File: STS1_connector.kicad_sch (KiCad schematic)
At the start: 2 parts

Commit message: Label RasPi Zero W pin header
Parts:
- added J2, J3: Conn_02x20_Odd_Even, symbol Connector_Generic:Conn_02x20_Odd_Even
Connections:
- net GND: now also J2.10 (Pin_10), J2.13 (Pin_13), J2.19 (Pin_19), J2.26 (Pin_26), J2.29 (Pin_29), J2.33 (Pin_33), J2.40 (Pin_40), J2.5 (Pin_5), J3.10 (Pin_10), J3.13 (Pin_13), J3.19 (Pin_19), J3.26 (Pin_26), J3.29 (Pin_29), J3.33 (Pin_33), J3.40 (Pin_40), J3.5 (Pin_5)
- new net 3V3: J2.2 (Pin_2), J3.18 (Pin_18), J3.2 (Pin_2)
- new net 5V: J3.1 (Pin_1), J3.3 (Pin_3)
- new net GPIO17: J2.12 (Pin_12), J3.12 (Pin_12)
- new net GPIO22: J2.16 (Pin_16), J3.16 (Pin_16)
- new net GPIO27: J2.14 (Pin_14), J3.14 (Pin_14)
- new net RX: J3.9 (Pin_9)
- new net SCL0: J2.6 (Pin_6)
- new net SDA0: J2.4 (Pin_4)
- new net TX: J3.7 (Pin_7)
- no-connect marks 0 -> 49
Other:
- note added: "CSBI connectors"
- note added: "EDU CSBI [1]"
- note added: "Pi HAT [2]"
- note added: "Pi HAT connector"
- note added: "Pi Zero W [3]"
- note added: "Pi Zero W connector"
- note added: "[1] https://github.com/SpaceTeam/STS1_EDU_Hardware [2] https://github.com/SpaceTeam/EDU_RASPI_HATS [3] https://pip-assets.raspberrypi.com/categories/592-raspberry-pi-zero-w/documents/RP-008368-DS-1-raspberry-pi-zero-w-reduced-schematics.pdf"

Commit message: Add 3V3 LDO: could be used to set EPS_BAT_GOOD high
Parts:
- J1: renamed from J2; footprint (none) -> Connector_PinHeader_2.00mm:PinHeader_2x20_P2.00mm_Vertical
- J2: renamed from J3; footprint (none) -> Connector_PinHeader_2.00mm:PinHeader_2x20_P2.00mm_Vertical

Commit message: Clean-up
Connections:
- net 3V3 renamed Pi_3V3
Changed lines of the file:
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@@
 		)
 	)
-	(global_label "3V3"
+	(global_label "Pi_3V3"
 		(shape input)
 		(at 242.57 44.45 0)
@@
 		)
 		(property "Intersheetrefs" "${INTERSHEET_REFS}"
-			(at 248.4086 44.45 0)
+			(at 251.251 44.45 0)
 			(hide yes)
 			(show_name no)
@@
 		)
 	)
-	(global_label "3V3"
+	(global_label "Pi_3V3"
 		(shape input)
 		(at 185.42 44.45 0)
@@
 		)
 		(property "Intersheetrefs" "${INTERSHEET_REFS}"
-			(at 191.2586 44.45 0)
+			(at 194.101 44.45 0)
 			(hide yes)
 			(show_name no)
@@
 		)
 	)
-	(global_label "3V3"
+	(global_label "Pi_3V3"
 		(shape input)
 		(at 242.57 64.77 0)
@@
 		)
 		(property "Intersheetrefs" "${INTERSHEET_REFS}"
-			(at 248.4086 64.77 0)
-			(hide yes)
-			(show_name no)
+			(at 251.251 64.77 0)
+			(hide yes)
+			(show_name no)

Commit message: Position PiHat, Raspberry Zero, and battery holder
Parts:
- J1, J2: footprint Connector_PinHeader_2.00mm:PinHeader_2x20_P2.00mm_Vertical -> Connector_PinHeader_2.54mm:PinHeader_2x20_P2.54mm_Vertical
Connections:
- net 5V is gone; now on net VBUS: J2.1 (Pin_1), J2.3 (Pin_3)
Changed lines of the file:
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@@
 		)
 	)
-	(global_label "5V"
+	(global_label "VBUS"
 		(shape input)
 		(at 222.25 44.45 180)
@@
 		)
 		(property "Intersheetrefs" "${INTERSHEET_REFS}"
-			(at 217.6209 44.45 0)
+			(at 215.0204 44.45 0)
 			(hide yes)
 			(show_name no)
@@
 			)
 		)
-		(property "Footprint" "Connector_PinHeader_2.00mm:PinHeader_2x20_P2.00mm_Vertical"
+		(property "Footprint" "Connector_PinHeader_2.54mm:PinHeader_2x20_P2.54mm_Vertical"
 			(at 173.99 67.31 0)
 			(hide yes)
@@
 			)
 		)
-		(property "Footprint" "Connector_PinHeader_2.00mm:PinHeader_2x20_P2.00mm_Vertical"
+		(property "Footprint" "Connector_PinHeader_2.54mm:PinHeader_2x20_P2.54mm_Vertical"
 			(at 231.14 67.31 0)
 			(hide yes)

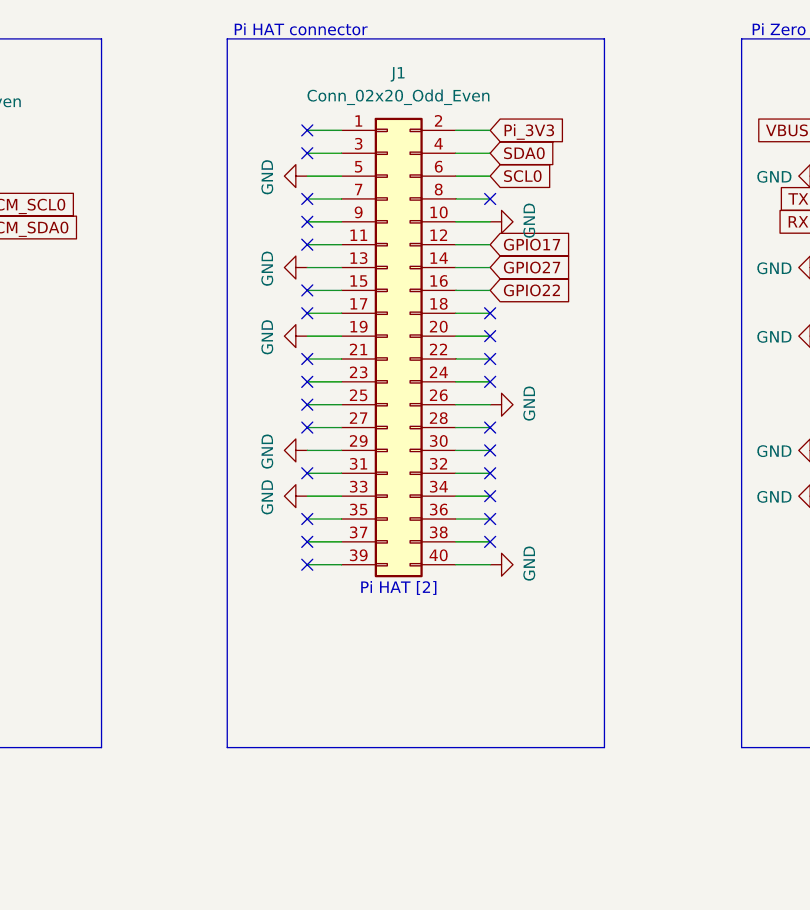
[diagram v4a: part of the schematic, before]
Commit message: Fix the labels on PiHAT connector
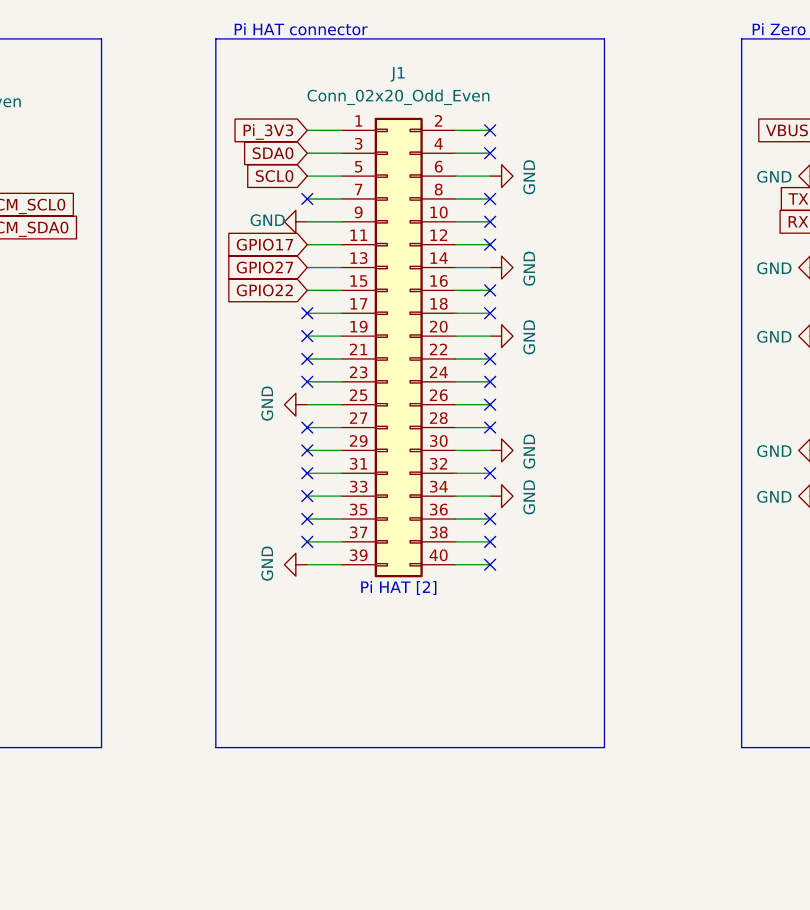
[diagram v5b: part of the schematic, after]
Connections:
- net GND: now also J1.14 (Pin_14), J1.20 (Pin_20), J1.25 (Pin_25), J1.30 (Pin_30), J1.34 (Pin_34), J1.39 (Pin_39), J1.6 (Pin_6), J1.9 (Pin_9); no longer J1.10 (Pin_10), J1.13 (Pin_13), J1.19 (Pin_19), J1.26 (Pin_26), J1.29 (Pin_29), J1.33 (Pin_33), J1.40 (Pin_40), J1.5 (Pin_5)
- net GPIO17: now also J1.11 (Pin_11); no longer J1.12 (Pin_12)
- net GPIO22: now also J1.15 (Pin_15); no longer J1.16 (Pin_16)
- net GPIO27: now also J1.13 (Pin_13); no longer J1.14 (Pin_14)
- net Pi_3V3: now also J1.1 (Pin_1); no longer J1.2 (Pin_2)
- net SCL0: now also J1.5 (Pin_5); no longer J1.6 (Pin_6)
- net SDA0: now also J1.3 (Pin_3); no longer J1.4 (Pin_4)

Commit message: Finilize connection and placement of components
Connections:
- net UART_COBC_EDU_1 is gone; now on net Pi_RX: CSBI_1.45 (Pin_45), CSBI_1.46 (Pin_46)
- net UART_COBC_EDU_2 is gone; now on net Pi_TX: CSBI_1.43 (Pin_43), CSBI_1.44 (Pin_44)
- net RX renamed Pi_RX
- net TX renamed Pi_TX
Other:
- note added: "TX/RC on the connector should be w.r.t COBC"
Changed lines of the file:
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@@
 		)
 	)
+	(text "TX/RC on the connector should be w.r.t COBC"
+		(exclude_from_sim no)
+		(at 52.07 121.92 0)
+		(effects
+			(font
+				(size 1.27 1.27)
+			)
+		)
+	)
 	(text "Pi HAT connector"
 		(exclude_from_sim no)
@@
 	(wire
 		(pts
+			(xy 40.64 118.11) (xy 53.34 118.11)
+		)
+		(stroke
+			(width 0)
+			(type default)
+		)
+	)
+	(wire
+		(pts
 			(xy 238.76 85.09) (xy 242.57 85.09)
 		)
@@
 	(wire
 		(pts
+			(xy 40.64 115.57) (xy 52.07 115.57)
+		)
+		(stroke
+			(width 0)
+			(type default)
+		)
+	)
+	(wire
+		(pts
 			(xy 238.76 54.61) (xy 242.57 54.61)
 		)
@@
 		)
 	)
-	(global_label "RX"
+	(global_label "Pi_RX"
 		(shape input)
 		(at 222.25 54.61 180)
@@
 		)
 		(property "Intersheetrefs" "${INTERSHEET_REFS}"
-			(at 217.4395 54.61 0)
+			(at 214.5971 54.61 0)
 			(hide yes)
 			(show_name no)
@@
 		)
 	)
-	(global_label "TX"
+	(global_label "Pi_TX"
 		(shape input)
 		(at 222.25 52.07 180)
@@
 		)
 		(property "Intersheetrefs" "${INTERSHEET_REFS}"
-			(at 217.7419 52.07 0)
+			(at 214.8995 52.07 0)
 			(hide yes)
 			(show_name no)
@@
 		)
 	)
+	(global_label "UART_COBC_EDU_2"
+		(shape input)
+		(at 52.07 115.57 0)
+		(fields_autoplaced yes)
+		(effects
+			(font
+				(size 1.27 1.27)
+			)
+			(justify left)
+		)
+		(property "Intersheetrefs" "${INTERSHEET_REFS}"
+			(at 72.06 115.57 0)
+			(hide yes)
+			(show_name no)
+			(do_not_autoplace no)
+			(effects
+				(font
+					(size 1.27 1.27)
+				)
+				(justify left)
+			)
+		)
+	)
 	(global_label "EDU_SPI_5"
 		(shape input)
@@
 		)
 	)
+	(global_label "Pi_TX"
+		(shape input)
+		(at 40.64 115.57 180)
+		(fields_autoplaced yes)
+		(effects
+			(font
+				(size 1.27 1.27)
+			)
+			(justify right)
+		)
+		(property "Intersheetrefs" "${INTERSHEET_REFS}"
+			(at 33.2895 115.57 0)
+			(hide yes)
+			(show_name no)
+			(do_not_autoplace no)
+			(effects
+				(font
+					(size 1.27 1.27)
+				)
+				(justify right)
+			)
+		)
+	)
 	(global_label "GPIO22"
 		(shape input)
@@
 		)
 	)
+	(global_label "Pi_RX"
+		(shape input)
+		(at 40.64 118.11 180)
+		(fields_autoplaced yes)
+		(effects
+			(font
+				(size 1.27 1.27)
+			)
+			(justify right)
+		)
+		(property "Intersheetrefs" "${INTERSHEET_REFS}"
+			(at 32.9871 118.11 0)
+			(hide yes)
+			(show_name no)
+			(do_not_autoplace no)
+			(effects
+				(font
+					(size 1.27 1.27)
+				)
+				(justify right)
+			)
+		)
+	)
 	(global_label "UART_COBC_EDU_1"
 		(shape input)
@@
 		)
 	)
+	(global_label "UART_COBC_EDU_1"
+		(shape input)
+		(at 52.07 118.11 0)
+		(fields_autoplaced yes)
+		(effects
+			(font
+				(size 1.27 1.27)
+			)
+			(justify left)
+		)
+		(property "Intersheetrefs" "${INTERSHEET_REFS}"
+			(at 72.06 118.11 0)
+			(hide yes)
+			(show_name no)
+			(do_not_autoplace no)
+			(effects
+				(font
+					(size 1.27 1.27)
+				)
+				(justify left)
+			)
+		)
+	)
 	(symbol
 		(lib_id "Connector_Generic:Conn_02x25_Odd_Even")
@@
 		(in_pos_files yes)
 		(dnp no)
-		(property "Reference" "#PWR018"
+		(property "Reference" "#PWR023"
 			(at 191.77 80.01 0)
 			(hide yes)
@@
 			(project "STS1_EEE"
 				(path "/81e05c2b-9a2c-430f-84ee-6a59968cd49a/00000000-0000-0000-0000-000059c45183"
-					(reference "#PWR018")
+					(reference "#PWR023")
 					(unit 1)
 				)
@@
 		(in_pos_files yes)
 		(dnp no)
-		(property "Reference" "#PWR019"
+		(property "Reference" "#PWR022"
 			(at 191.77 67.31 0)
 			(hide yes)
@@
 			(project "STS1_EEE"
 				(path "/81e05c2b-9a2c-430f-84ee-6a59968cd49a/00000000-0000-0000-0000-000059c45183"
-					(reference "#PWR019")
+					(reference "#PWR022")
 					(unit 1)
 				)
@@
 		(in_pos_files yes)
 		(dnp no)
-		(property "Reference" "#PWR020"
+		(property "Reference" "#PWR021"
 			(at 191.77 59.69 0)
 			(hide yes)
@@
 			(project "STS1_EEE"
 				(path "/81e05c2b-9a2c-430f-84ee-6a59968cd49a/00000000-0000-0000-0000-000059c45183"
-					(reference "#PWR020")
+					(reference "#PWR021")
 					(unit 1)
 				)
@@
 		(in_pos_files yes)
 		(dnp no)
-		(property "Reference" "#PWR023"
+		(property "Reference" "#PWR018"
 			(at 158.75 74.93 0)
 			(hide yes)
@@
 			(project "STS1_EEE"
 				(path "/81e05c2b-9a2c-430f-84ee-6a59968cd49a/00000000-0000-0000-0000-000059c45183"
-					(reference "#PWR023")
+					(reference "#PWR018")
 					(unit 1)
 				)
@@
 		(in_pos_files yes)
 		(dnp no)
-		(property "Reference" "#PWR017"
+		(property "Reference" "#PWR024"
 			(at 191.77 85.09 0)
 			(hide yes)
@@
 			(project "STS1_EEE"
 				(path "/81e05c2b-9a2c-430f-84ee-6a59968cd49a/00000000-0000-0000-0000-000059c45183"
-					(reference "#PWR017")
+					(reference "#PWR024")
 					(unit 1)
 				)
@@
 		(in_pos_files yes)
 		(dnp no)
-		(property "Reference" "#PWR022"
+		(property "Reference" "#PWR017"
 			(at 158.75 54.61 0)
 			(hide yes)
@@
 			(project "STS1_EEE"
 				(path "/81e05c2b-9a2c-430f-84ee-6a59968cd49a/00000000-0000-0000-0000-000059c45183"
-					(reference "#PWR022")
+					(reference "#PWR017")
 					(unit 1)
 				)
@@
 		(in_pos_files yes)
 		(dnp no)
-		(property "Reference" "#PWR024"
+		(property "Reference" "#PWR019"
 			(at 158.75 92.71 0)
 			(hide yes)
@@
 			(project "STS1_EEE"
 				(path "/81e05c2b-9a2c-430f-84ee-6a59968cd49a/00000000-0000-0000-0000-000059c45183"
-					(reference "#PWR024")
+					(reference "#PWR019")
 					(unit 1)
 				)
@@
 		(in_pos_files yes)
 		(dnp no)
-		(property "Reference" "#PWR021"
+		(property "Reference" "#PWR020"
 			(at 191.77 49.53 0)
 			(hide yes)
@@
 			(project "STS1_EEE"
 				(path "/81e05c2b-9a2c-430f-84ee-6a59968cd49a/00000000-0000-0000-0000-000059c45183"
-					(reference "#PWR021")
+					(reference "#PWR020")
 					(unit 1)
 				)

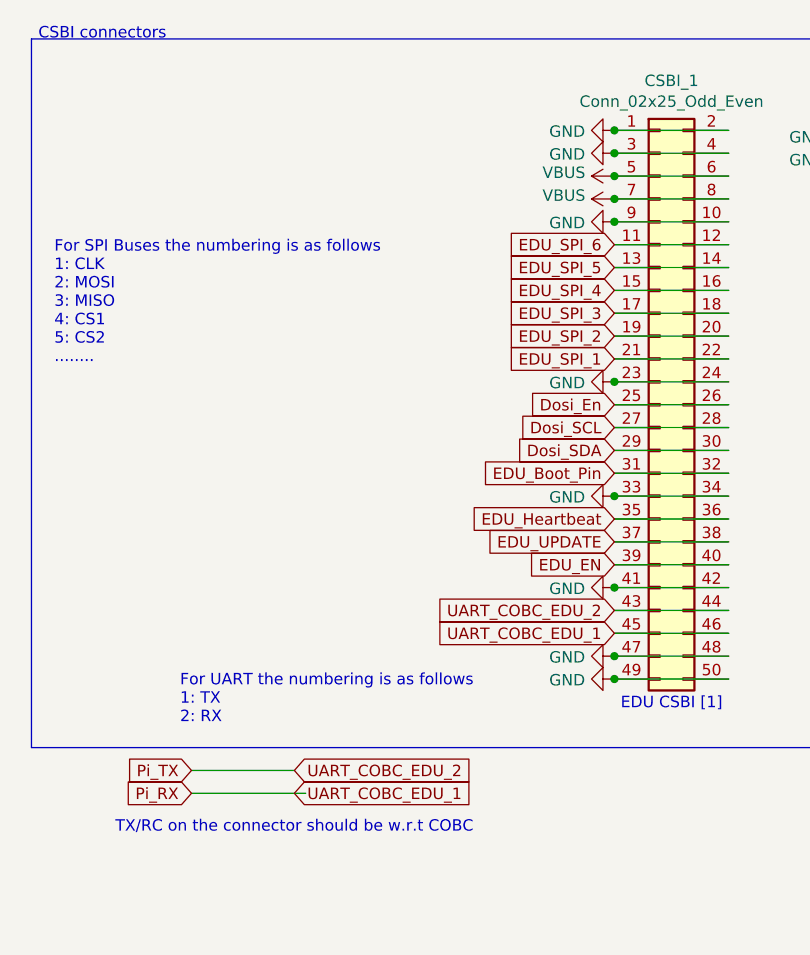
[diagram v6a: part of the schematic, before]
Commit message: Fix ERC errors
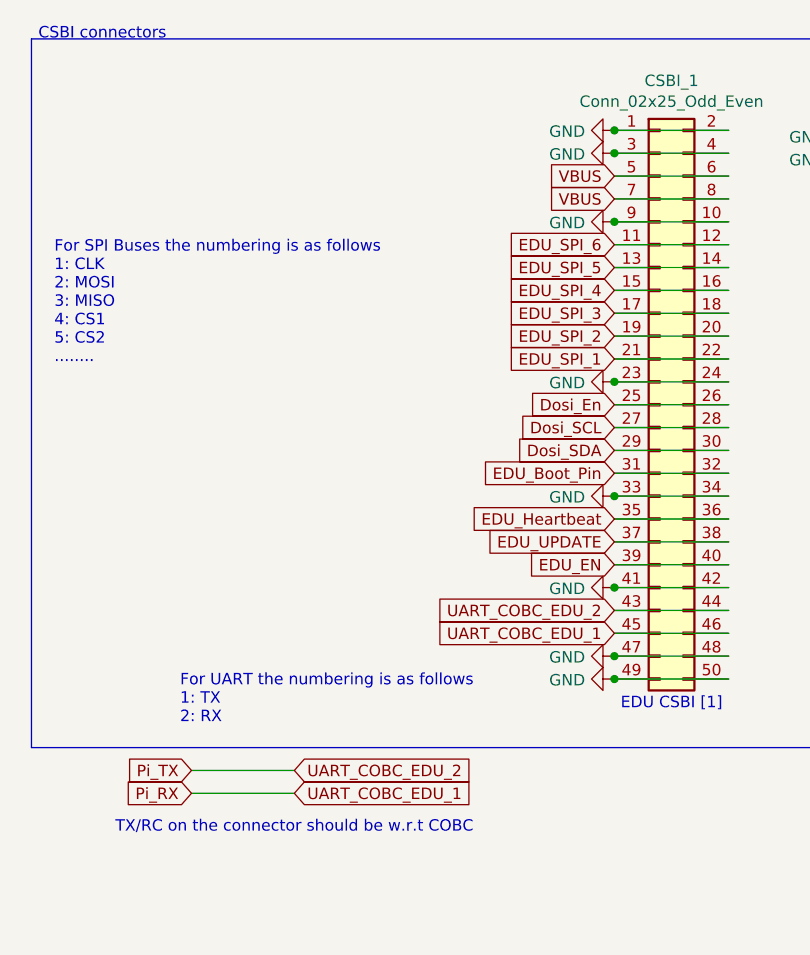
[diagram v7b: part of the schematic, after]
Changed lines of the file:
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@@
-	)
-	(junction
-		(at 87.63 52.07)
-		(diameter 0)
-		(color 0 0 0 0)
 	)
 	(junction
@@
 	)
 	(junction
-		(at 87.63 49.53)
-		(diameter 0)
-		(color 0 0 0 0)
-	)
-	(junction
 		(at 87.63 72.39)
 		(diameter 0)
@@
 	(wire
 		(pts
-			(xy 40.64 118.11) (xy 53.34 118.11)
-		)
-		(stroke
-			(width 0)
-			(type default)
-		)
-	)
-	(wire
-		(pts
 			(xy 238.76 85.09) (xy 242.57 85.09)
 		)
@@
 	(wire
 		(pts
+			(xy 40.64 118.11) (xy 52.07 118.11)
+		)
+		(stroke
+			(width 0)
+			(type default)
+		)
+	)
+	(wire
+		(pts
 			(xy 181.61 77.47) (xy 185.42 77.47)
 		)
@@
 		)
 	)
+	(global_label "VBUS"
+		(shape input)
+		(at 87.63 49.53 180)
+		(fields_autoplaced yes)
+		(effects
+			(font
+				(size 1.27 1.27)
+			)
+			(justify right)
+		)
+		(property "Intersheetrefs" "${INTERSHEET_REFS}"
+			(at 80.4004 49.53 0)
+			(hide yes)
+			(show_name no)
+			(do_not_autoplace no)
+			(effects
+				(font
+					(size 1.27 1.27)
+				)
+				(justify right)
+			)
+		)
+	)
 	(global_label "GPIO17"
 		(shape input)
@@
 		(property "Intersheetrefs" "${INTERSHEET_REFS}"
 			(at 75.3272 64.8494 0)
+			(hide yes)
+			(show_name no)
+			(do_not_autoplace no)
+			(effects
+				(font
+					(size 1.27 1.27)
+				)
+				(justify right)
+			)
+		)
+	)
+	(global_label "VBUS"
+		(shape input)
+		(at 87.63 52.07 180)
+		(fields_autoplaced yes)
+		(effects
+			(font
+				(size 1.27 1.27)
+			)
+			(justify right)
+		)
+		(property "Intersheetrefs" "${INTERSHEET_REFS}"
+			(at 80.4004 52.07 0)
 			(hide yes)
 			(show_name no)
@@
 					(unit 1)
 				)
-			)
-		)
-	)
-	(symbol
-		(lib_id "power:VBUS")
-		(at 87.63 49.53 90)
-		(unit 1)
-		(body_style 1)
-		(exclude_from_sim no)
-		(in_bom yes)
-		(on_board yes)
-		(in_pos_files yes)
-		(dnp no)
-		(property "Reference" "#PWR07"
-			(at 91.44 49.53 0)
-			(hide yes)
-			(show_name no)
-			(do_not_autoplace no)
-			(effects
-				(font
-					(size 1.27 1.27)
-				)
-			)
-		)
-		(property "Value" "VBUS"
-			(at 84.4042 49.149 90)
-			(show_name no)
-			(do_not_autoplace no)
-			(effects
-				(font
-					(size 1.27 1.27)
-				)
-				(justify left)
-			)
-		)
-		(property "Footprint" ""
-			(at 87.63 49.53 0)
-			(hide yes)
-			(show_name no)
-			(do_not_autoplace no)
-			(effects
-				(font
-					(size 1.27 1.27)
-				)
-			)
-		)
-		(property "Datasheet" ""
-			(at 87.63 49.53 0)
-			(hide yes)
-			(show_name no)
-			(do_not_autoplace no)
-			(effects
-				(font
-					(size 1.27 1.27)
-				)
-			)
-		)
-		(property "Description" ""
-			(at 87.63 49.53 0)
-			(show_name no)
-			(do_not_autoplace no)
-			(effects
-				(font
-					(size 1.27 1.27)
-				)
-			)
-		)
-		(pin "1"
-		)
-		(instances
-			(project "STS1_EEE"
-				(path "/81e05c2b-9a2c-430f-84ee-6a59968cd49a/00000000-0000-0000-0000-000059c45183"
-					(reference "#PWR07")
-					(unit 1)
-				)
-			)
-		)
-	)
-	(symbol
-		(lib_id "power:VBUS")
-		(at 87.63 52.07 90)
-		(unit 1)
-		(body_style 1)
-		(exclude_from_sim no)
-		(in_bom yes)
-		(on_board yes)
-		(in_pos_files yes)
-		(dnp no)
-		(property "Reference" "#PWR08"
-			(at 91.44 52.07 0)
-			(hide yes)
-			(show_name no)
-			(do_not_autoplace no)
-			(effects
-				(font
-					(size 1.27 1.27)
-				)
-			)
-		)
-		(property "Value" "VBUS"
-			(at 84.4042 51.689 90)
-			(show_name no)
-			(do_not_autoplace no)
-			(effects
-				(font
-					(size 1.27 1.27)
-				)
-				(justify left)
-			)
-		)
-		(property "Footprint" ""
-			(at 87.63 52.07 0)
-			(hide yes)
-			(show_name no)
-			(do_not_autoplace no)
-			(effects
-				(font
-					(size 1.27 1.27)
-				)
-			)
-		)
-		(property "Datasheet" ""
-			(at 87.63 52.07 0)
-			(hide yes)
-			(show_name no)
-			(do_not_autoplace no)
-			(effects
-				(font
-					(size 1.27 1.27)
-				)
-			)
-		)
-		(property "Description" ""
-			(at 87.63 52.07 0)
-			(show_name no)
-			(do_not_autoplace no)
-			(effects
-				(font
-					(size 1.27 1.27)
-				)
-			)
-		)
-		(pin "1"
-		)
-		(instances
-			(project "STS1_EEE"
-				(path "/81e05c2b-9a2c-430f-84ee-6a59968cd49a/00000000-0000-0000-0000-000059c45183"
-					(reference "#PWR08")
-					(unit 1)
-				)
